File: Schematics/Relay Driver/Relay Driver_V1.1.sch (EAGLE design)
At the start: 19 parts, among them IC1 74AC04N

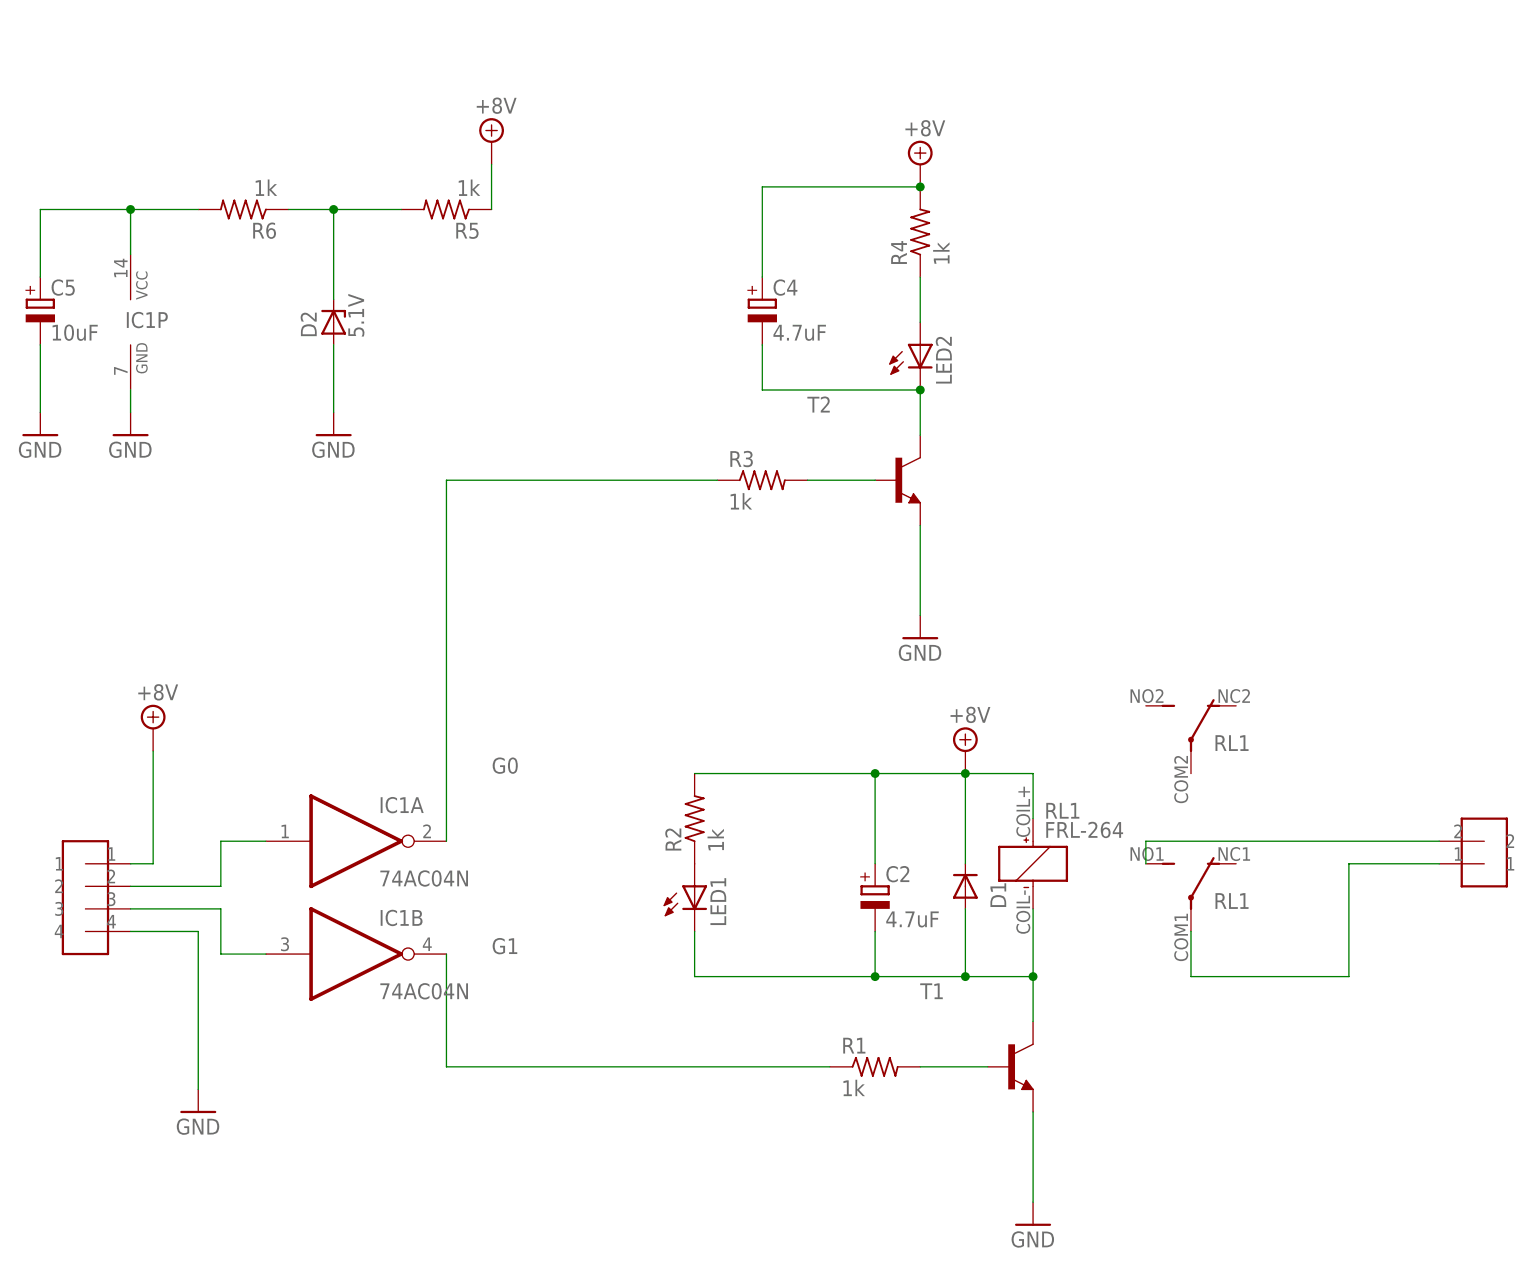
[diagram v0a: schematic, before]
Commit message: Updated relay board, updated documentation
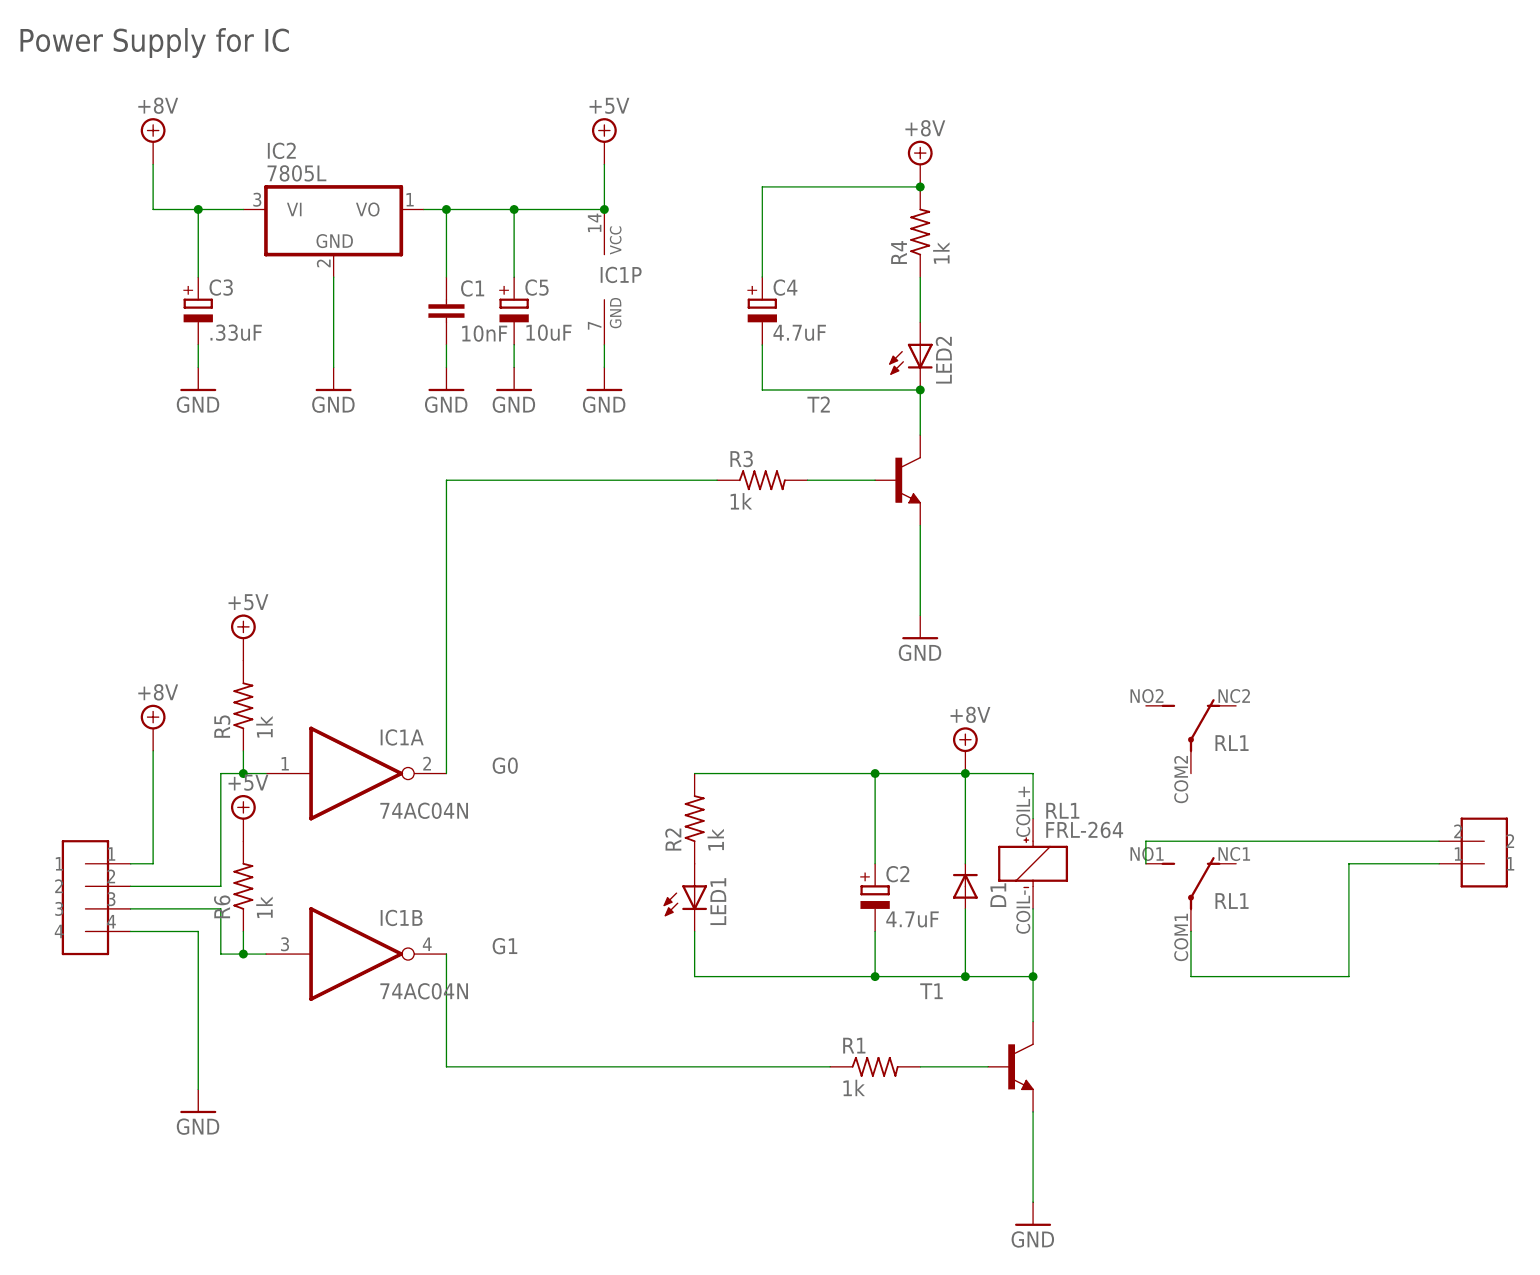
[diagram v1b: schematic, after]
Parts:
- removed D2: 5.1V, diode:ZENER-DIODEDO35Z10
- added C1: 10nF, rcl:C-EU075-042X103
- added C3: .33uF, rcl:CPOL-EUE3.5-10
- added IC2: 7805L, linear:7805L
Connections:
- removed net N$12: C5.+, IC1P.VCC, R6.2
- removed net N$13: D2.C, R5.2, R6.1
- new net +5V: C1.1, C5.+, IC1P.VCC, IC2.VO, R5.2, R6.2
- net +8V: now also C3.+, IC2.VI; no longer R5.1
- net GND: now also C1.2, C3.-, IC2.GND; no longer D2.A
- net N$6: now also R5.1
- net N$8: now also R6.1
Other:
- note added: "Power Supply for IC"
- moved on the sheet: C5, IC1A, IC1P, R5, R6
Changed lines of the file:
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@@
 <setting verticaltext="up"/>
 </settings>
-<grid distance="0.1" unitdist="inch" unit="inch" style="lines" multiple="1" display="no" altdistance="0.01" altunitdist="inch" altunit="inch"/>
+<grid distance="0.1" unitdist="inch" unit="inch" style="lines" multiple="1" display="yes" altdistance="0.01" altunitdist="inch" altunit="inch"/>
 <layers>
 <layer number="1" name="Top" color="4" fill="1" visible="no" active="no"/>
@@
 <part name="RL1" library="relay" deviceset="FRL-264" device=""/>
 <part name="IC1" library="74xx-eu" deviceset="74*04" device="N" technology="AC"/>
-<part name="D2" library="diode" deviceset="ZENER-DIODE" device="DO35Z10" value="5.1V"/>
-<part name="R5" library="rcl" deviceset="R-US_" device="0613/5V" value="1k"/>
-<part name="R6" library="rcl" deviceset="R-US_" device="0613/5V" value="1k"/>
 <part name="C5" library="rcl" deviceset="CPOL-EU" device="E3.5-10" value="10uF"/>
 <part name="SUPPLY4" library="supply2" deviceset="+8V" device=""/>
@@
 <part name="GND7" library="supply1" deviceset="GND" device=""/>
 <part name="GND8" library="supply1" deviceset="GND" device=""/>
+<part name="IC2" library="linear" deviceset="78*" device="L" technology="05"/>
+<part name="C1" library="rcl" deviceset="C-EU" device="075-042X103" value="10nF"/>
+<part name="C3" library="rcl" deviceset="CPOL-EU" device="E3.5-10" value=".33uF"/>
+<part name="GND1" library="supply1" deviceset="GND" device=""/>
+<part name="GND4" library="supply1" deviceset="GND" device=""/>
+<part name="SUPPLY5" library="supply2" deviceset="+5V" device=""/>
+<part name="R5" library="rcl" deviceset="R-US_" device="0613/5V" value="1k"/>
+<part name="R6" library="rcl" deviceset="R-US_" device="0613/5V" value="1k"/>
+<part name="SUPPLY6" library="supply2" deviceset="+5V" device=""/>
+<part name="SUPPLY7" library="supply2" deviceset="+5V" device=""/>
 </parts>
 <sheets>
 <sheet>
 <plain>
+<text x="35.56" y="182.88" size="2.54" layer="97">Power Supply for IC</text>
 </plain>
 <instances>
@@
 <instance part="RL1" gate="G$2" x="167.64" y="86.36"/>
 <instance part="RL1" gate="G$3" x="167.64" y="104.14"/>
-<instance part="IC1" gate="A" x="73.66" y="93.98"/>
+<instance part="IC1" gate="A" x="73.66" y="101.6"/>
 <instance part="IC1" gate="B" x="73.66" y="81.28"/>
-<instance part="IC1" gate="P" x="48.26" y="152.4"/>
-<instance part="D2" gate="G$1" x="71.12" y="152.4" rot="R90"/>
-<instance part="R5" gate="G$1" x="83.82" y="165.1" rot="R180"/>
-<instance part="R6" gate="G$1" x="60.96" y="165.1" rot="R180"/>
-<instance part="C5" gate="G$1" x="38.1" y="154.94"/>
-<instance part="SUPPLY4" gate="+8V" x="88.9" y="172.72"/>
-<instance part="GND6" gate="1" x="48.26" y="139.7"/>
-<instance part="GND7" gate="1" x="38.1" y="139.7"/>
-<instance part="GND8" gate="1" x="71.12" y="139.7"/>
+<instance part="IC1" gate="P" x="101.6" y="157.48"/>
+<instance part="C5" gate="G$1" x="91.44" y="154.94"/>
+<instance part="SUPPLY4" gate="+8V" x="50.8" y="172.72"/>
+<instance part="GND6" gate="1" x="101.6" y="144.78"/>
+<instance part="GND7" gate="1" x="91.44" y="144.78"/>
+<instance part="GND8" gate="1" x="71.12" y="144.78"/>
+<instance part="IC2" gate="A1" x="71.12" y="165.1"/>
+<instance part="C1" gate="G$1" x="83.82" y="154.94"/>
+<instance part="C3" gate="G$1" x="55.88" y="154.94"/>
+<instance part="GND1" gate="1" x="55.88" y="144.78"/>
+<instance part="GND4" gate="1" x="83.82" y="144.78"/>
+<instance part="SUPPLY5" gate="+5V" x="101.6" y="172.72"/>
+<instance part="R5" gate="G$1" x="60.96" y="109.22" rot="R90"/>
+<instance part="R6" gate="G$1" x="60.96" y="88.9" rot="R90"/>
+<instance part="SUPPLY6" gate="+5V" x="60.96" y="116.84"/>
+<instance part="SUPPLY7" gate="+5V" x="60.96" y="96.52"/>
 </instances>
 <busses>
@@
 <pinref part="C5" gate="G$1" pin="-"/>
 <pinref part="GND7" gate="1" pin="GND"/>
-<wire x1="38.1" y1="149.86" x2="38.1" y2="142.24" width="0.1524" layer="91"/>
-</segment>
-<segment>
-<pinref part="D2" gate="G$1" pin="A"/>
+<wire x1="91.44" y1="149.86" x2="91.44" y2="147.32" width="0.1524" layer="91"/>
+</segment>
+<segment>
 <pinref part="GND8" gate="1" pin="GND"/>
-<wire x1="71.12" y1="149.86" x2="71.12" y2="142.24" width="0.1524" layer="91"/>
+<pinref part="IC2" gate="A1" pin="GND"/>
+<wire x1="71.12" y1="157.48" x2="71.12" y2="147.32" width="0.1524" layer="91"/>
 </segment>
 <segment>
 <pinref part="IC1" gate="P" pin="GND"/>
 <pinref part="GND6" gate="1" pin="GND"/>
-<wire x1="48.26" y1="144.78" x2="48.26" y2="142.24" width="0.1524" layer="91"/>
+<wire x1="101.6" y1="149.86" x2="101.6" y2="147.32" width="0.1524" layer="91"/>
+</segment>
+<segment>
+<pinref part="C3" gate="G$1" pin="-"/>
+<pinref part="GND1" gate="1" pin="GND"/>
+<wire x1="55.88" y1="149.86" x2="55.88" y2="147.32" width="0.1524" layer="91"/>
+</segment>
+<segment>
+<pinref part="C1" gate="G$1" pin="2"/>
+<pinref part="GND4" gate="1" pin="GND"/>
+<wire x1="83.82" y1="149.86" x2="83.82" y2="147.32" width="0.1524" layer="91"/>
 </segment>
 </net>
@@
 <segment>
 <pinref part="R3" gate="G$1" pin="1"/>
-<wire x1="83.82" y1="93.98" x2="83.82" y2="134.62" width="0.1524" layer="91"/>
+<wire x1="83.82" y1="101.6" x2="83.82" y2="134.62" width="0.1524" layer="91"/>
 <wire x1="83.82" y1="134.62" x2="114.3" y2="134.62" width="0.1524" layer="91"/>
 <label x="88.9" y="101.6" size="1.778" layer="95"/>
@@
 </segment>
 <segment>
-<pinref part="R5" gate="G$1" pin="1"/>
-<wire x1="88.9" y1="165.1" x2="88.9" y2="170.18" width="0.1524" layer="91"/>
+<wire x1="50.8" y1="165.1" x2="50.8" y2="170.18" width="0.1524" layer="91"/>
 <pinref part="SUPPLY4" gate="+8V" pin="+8V"/>
+<pinref part="IC2" gate="A1" pin="VI"/>
+<wire x1="50.8" y1="165.1" x2="55.88" y2="165.1" width="0.1524" layer="91"/>
+<pinref part="C3" gate="G$1" pin="+"/>
+<wire x1="55.88" y1="165.1" x2="60.96" y2="165.1" width="0.1524" layer="91"/>
+<wire x1="55.88" y1="157.48" x2="55.88" y2="165.1" width="0.1524" layer="91"/>
+<junction x="55.88" y="165.1"/>
 </segment>
 </net>
@@
 <pinref part="U$1" gate="G$1" pin="2"/>
 <wire x1="48.26" y1="88.9" x2="58.42" y2="88.9" width="0.1524" layer="91"/>
-<wire x1="58.42" y1="88.9" x2="58.42" y2="93.98" width="0.1524" layer="91"/>
+<wire x1="58.42" y1="88.9" x2="58.42" y2="101.6" width="0.1524" layer="91"/>
 <pinref part="IC1" gate="A" pin="I"/>
-<wire x1="58.42" y1="93.98" x2="63.5" y2="93.98" width="0.1524" layer="91"/>
+<wire x1="58.42" y1="101.6" x2="60.96" y2="101.6" width="0.1524" layer="91"/>
+<pinref part="R5" gate="G$1" pin="1"/>
+<wire x1="60.96" y1="101.6" x2="63.5" y2="101.6" width="0.1524" layer="91"/>
+<wire x1="60.96" y1="104.14" x2="60.96" y2="101.6" width="0.1524" layer="91"/>
+<junction x="60.96" y="101.6"/>
 </segment>
 </net>
@@
 <segment>
 <pinref part="IC1" gate="B" pin="I"/>
-<wire x1="63.5" y1="81.28" x2="58.42" y2="81.28" width="0.1524" layer="91"/>
+<wire x1="63.5" y1="81.28" x2="60.96" y2="81.28" width="0.1524" layer="91"/>
+<wire x1="60.96" y1="81.28" x2="58.42" y2="81.28" width="0.1524" layer="91"/>
 <wire x1="58.42" y1="81.28" x2="58.42" y2="86.36" width="0.1524" layer="91"/>
 <pinref part="U$1" gate="G$1" pin="3"/>
 <wire x1="58.42" y1="86.36" x2="48.26" y2="86.36" width="0.1524" layer="91"/>
-</segment>
-</net>
-<net name="N$12" class="0">
+<pinref part="R6" gate="G$1" pin="1"/>
+<wire x1="60.96" y1="83.82" x2="60.96" y2="81.28" width="0.1524" layer="91"/>
+<junction x="60.96" y="81.28"/>
+</segment>
+</net>
+<net name="+5V" class="0">
 <segment>
 <pinref part="C5" gate="G$1" pin="+"/>
-<wire x1="38.1" y1="157.48" x2="38.1" y2="165.1" width="0.1524" layer="91"/>
+<wire x1="91.44" y1="157.48" x2="91.44" y2="165.1" width="0.1524" layer="91"/>
 <pinref part="IC1" gate="P" pin="VCC"/>
-<wire x1="38.1" y1="165.1" x2="48.26" y2="165.1" width="0.1524" layer="91"/>
-<wire x1="48.26" y1="165.1" x2="48.26" y2="160.02" width="0.1524" layer="91"/>
+<wire x1="91.44" y1="165.1" x2="101.6" y2="165.1" width="0.1524" layer="91"/>
+<pinref part="IC2" gate="A1" pin="VO"/>
+<wire x1="91.44" y1="165.1" x2="83.82" y2="165.1" width="0.1524" layer="91"/>
+<junction x="91.44" y="165.1"/>
+<pinref part="C1" gate="G$1" pin="1"/>
+<wire x1="83.82" y1="165.1" x2="81.28" y2="165.1" width="0.1524" layer="91"/>
+<wire x1="83.82" y1="157.48" x2="83.82" y2="165.1" width="0.1524" layer="91"/>
+<junction x="83.82" y="165.1"/>
+<pinref part="SUPPLY5" gate="+5V" pin="+5V"/>
+<wire x1="101.6" y1="170.18" x2="101.6" y2="165.1" width="0.1524" layer="91"/>
+<junction x="101.6" y="165.1"/>
+</segment>
+<segment>
+<pinref part="R5" gate="G$1" pin="2"/>
+<pinref part="SUPPLY6" gate="+5V" pin="+5V"/>
+</segment>
+<segment>
 <pinref part="R6" gate="G$1" pin="2"/>
-<wire x1="55.88" y1="165.1" x2="48.26" y2="165.1" width="0.1524" layer="91"/>
-<junction x="48.26" y="165.1"/>
-</segment>
-</net>
-<net name="N$13" class="0">
-<segment>
-<pinref part="R6" gate="G$1" pin="1"/>
-<pinref part="R5" gate="G$1" pin="2"/>
-<wire x1="66.04" y1="165.1" x2="71.12" y2="165.1" width="0.1524" layer="91"/>
-<pinref part="D2" gate="G$1" pin="C"/>
-<wire x1="71.12" y1="165.1" x2="78.74" y2="165.1" width="0.1524" layer="91"/>
-<wire x1="71.12" y1="154.94" x2="71.12" y2="165.1" width="0.1524" layer="91"/>
-<junction x="71.12" y="165.1"/>
-</segment>
-</net>
+<pinref part="SUPPLY7" gate="+5V" pin="+5V"/>
+</segment>
+</net>
